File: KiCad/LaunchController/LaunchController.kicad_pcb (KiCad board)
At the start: 2 copper layers, 150 x 100 mm, 162 parts, among them J1 CONN_ICSP, J10 CONN_AUDIO, J11 RJ45, J12 CONN_SPEAKER, J2 CONN_USB, J3 USB_B_Micro, J4 DC_IN, J5 TO_CONVERTER, J6 FROM_CONVERTER, J7 CONN_STATUS_PANEL, J8 CONN_PANEL_BAORD_2, J9 CONN_PANEL_BAORD_1, Q1 TJ8S06M3L, Q2 TJ8S06M3L, Q3 2SC3325-Y, SW1 SW_Push, SW11 SW_Push, SW12 SW_Push, SW13 SW_Push, SW14 SW_Push, SW15 SW_Push, SW16 SW_Push, SW17 SW_Push, SW18 SW_Push, SW19 SW_Push, SW2 SW_Push, SW20 SW_Push, SW21 SW_Push, SW22 SW_Push, SW23 SW_Push, SW24 SW_Push, SW25 SW_Push, U1 FT232RL, U2 ATMEGA2560-16AUR, U3 NJM7805SDL1, U4 INA219BIDCNT, U5 INA219BIDCNT, U6 DFPlayer, U7 24LC256, U8 LTC485CN8#PBF, Y1 HUSG-16.000-20

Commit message: ロードスイッチ駆動用のトランジスタのベース抵抗を10kRに修正
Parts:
- R14: value 22kR -> 10kR
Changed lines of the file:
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@@
         (effects (font (size 1 1) (thickness 0.15)))
     )
-    (fp_text value "22kR" (at 0 1.43 180) (layer "F.Fab")
+    (fp_text value "10kR" (at 0 1.43 180) (layer "F.Fab")
         (effects (font (size 1 1) (thickness 0.15)))
     )

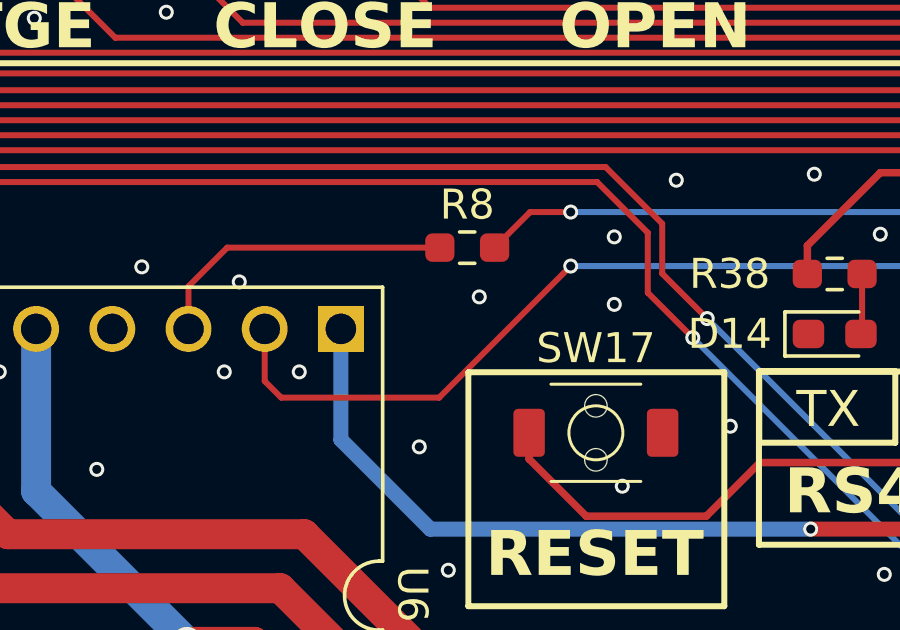
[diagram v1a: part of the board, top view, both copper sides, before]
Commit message: DFPlayerのTXにも抵抗を追加
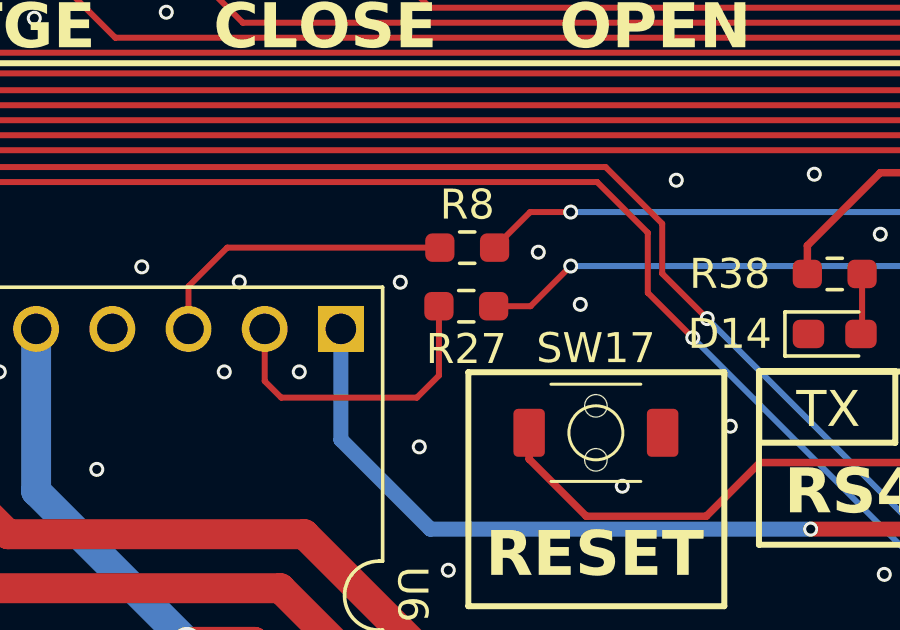
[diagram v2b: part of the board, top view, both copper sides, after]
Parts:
- added R27: 1kR, Resistor_SMD:R_0603_1608Metric_Pad0.98x0.95mm_HandSolder, F.Cu at (73.2, 88.2)
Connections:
- U2 pad 13: UART2_TX -> Net-(U2-PH1)
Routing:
- net UART2_TX: track 84.5 -> 10.4 mm, vias 2 -> 0
- net Net-(U2-PH1): track 0.00 -> 73.6 mm, vias 0 -> 2
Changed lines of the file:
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@@
   (net 165 "CONN_LED_POWER")
   (net 166 "CONN_LED_FB_SHIFT")
+  (net 167 "Net-(U2-PH1)")
   (footprint "Capacitor_SMD:C_0603_1608Metric_Pad1.08x0.95mm_HandSolder" (layer "F.Cu")
     (at 109.840587 69.251913 45)
@@
       (net 60 "Net-(U2-PH0)") (pinfunction "PH0") (pintype "bidirectional"))
     (pad "13" smd roundrect (at -7.6625 0 225) (size 1.475 0.3) (layers "F.Cu" "F.Paste" "F.Mask") (roundrect_rratio 0.25)
-      (net 100 "UART2_TX") (pinfunction "PH1") (pintype "bidirectional"))
+      (net 167 "Net-(U2-PH1)") (pinfunction "PH1") (pintype "bidirectional"))
     (pad "14" smd roundrect (at -7.6625 0.5 225) (size 1.475 0.3) (layers "F.Cu" "F.Paste" "F.Mask") (roundrect_rratio 0.25)
       (net 79 "CONN_LED_FB_PURGE") (pinfunction "PH2") (pintype "bidirectional"))
@@
     )
   )
+  (footprint "Resistor_SMD:R_0603_1608Metric_Pad0.98x0.95mm_HandSolder" (layer "F.Cu")
+    (at 73.2 88.2 180)
+    (descr "Resistor SMD 0603 (1608 Metric), square (rectangular) end terminal, IPC_7351 nominal with elongated pad for handsoldering. (Body size source: IPC-SM-782 page 72, https://www.pcb-3d.com/wordpress/wp-content/uploads/ipc-sm-782a_amendment_1_and_2.pdf), generated with kicad-footprint-generator")
+    (tags "resistor handsolder")
+    (property "LCSC" "")
+    (property "Sheetfile" "LaunchController.kicad_sch")
+    (property "Sheetname" "")
+    (property "ki_description" "Resistor, small symbol")
+    (property "ki_keywords" "R resistor")
+    (attr smd)
+    (fp_text reference "R27" (at 0 -1.43) (layer "F.SilkS")
+        (effects (font (size 1 1) (thickness 0.15)))
+    )
+    (fp_text value "1kR" (at 0 1.43) (layer "F.Fab")
+        (effects (font (size 1 1) (thickness 0.15)))
+    )
+    (fp_text user "${REFERENCE}" (at 0 0) (layer "F.Fab")
+        (effects (font (size 0.4 0.4) (thickness 0.06)))
+    )
+    (fp_line (start -0.254724 -0.5225) (end 0.254724 -0.5225)
+      (stroke (width 0.12) (type solid)) (layer "F.SilkS"))
+    (fp_line (start -0.254724 0.5225) (end 0.254724 0.5225)
+      (stroke (width 0.12) (type solid)) (layer "F.SilkS"))
+    (fp_line (start -1.65 -0.73) (end 1.65 -0.73)
+      (stroke (width 0.05) (type solid)) (layer "F.CrtYd"))
+    (fp_line (start -1.65 0.73) (end -1.65 -0.73)
+      (stroke (width 0.05) (type solid)) (layer "F.CrtYd"))
+    (fp_line (start 1.65 -0.73) (end 1.65 0.73)
+      (stroke (width 0.05) (type solid)) (layer "F.CrtYd"))
+    (fp_line (start 1.65 0.73) (end -1.65 0.73)
+      (stroke (width 0.05) (type solid)) (layer "F.CrtYd"))
+    (fp_line (start -0.8 -0.4125) (end 0.8 -0.4125)
+      (stroke (width 0.1) (type solid)) (layer "F.Fab"))
+    (fp_line (start -0.8 0.4125) (end -0.8 -0.4125)
+      (stroke (width 0.1) (type solid)) (layer "F.Fab"))
+    (fp_line (start 0.8 -0.4125) (end 0.8 0.4125)
+      (stroke (width 0.1) (type solid)) (layer "F.Fab"))
+    (fp_line (start 0.8 0.4125) (end -0.8 0.4125)
+      (stroke (width 0.1) (type solid)) (layer "F.Fab"))
+    (pad "1" smd roundrect (at -0.9125 0 180) (size 0.975 0.95) (layers "F.Cu" "F.Paste" "F.Mask") (roundrect_rratio 0.25)
+      (net 167 "Net-(U2-PH1)") (pintype "passive"))
+    (pad "2" smd roundrect (at 0.9125 0 180) (size 0.975 0.95) (layers "F.Cu" "F.Paste" "F.Mask") (roundrect_rratio 0.25)
+      (net 100 "UART2_TX") (pintype "passive"))
+    (model "${KICAD6_3DMODEL_DIR}/Resistor_SMD.3dshapes/R_0603_1608Metric.wrl"
+      (offset (xyz 0 0 0))
+      (scale (xyz 1 1 1))
+      (rotate (xyz 0 0 0))
+    )
+  )
   (footprint "LED_SMD:LED_0603_1608Metric_Pad1.05x0.95mm_HandSolder" (layer "F.Cu")
     (at 76.735 75.75 90)
@@
   (via (at 139.4 47.4) (size 0.5) (drill 0.3) (layers "F.Cu" "B.Cu") (free) (net 1))
   (via (at 103 104.25) (size 0.5) (drill 0.3) (layers "F.Cu" "B.Cu") (free) (net 1))
-  (via (at 78.133174 85.888716) (size 0.5) (drill 0.3) (layers "F.Cu" "B.Cu") (free) (net 1))
+  (via (at 75.6 86.4) (size 0.5) (drill 0.3) (layers "F.Cu" "B.Cu") (free) (net 1))
   (via (at 58.8 78.6) (size 0.5) (drill 0.3) (layers "F.Cu" "B.Cu") (free) (net 1))
   (via (at 122.883174 107.638716) (size 0.5) (drill 0.3) (layers "F.Cu" "B.Cu") (free) (net 1))
@@
   (via (at 94.6 47.2) (size 0.5) (drill 0.3) (layers "F.Cu" "B.Cu") (free) (net 1))
   (via (at 165.883174 90.138716) (size 0.5) (drill 0.3) (layers "F.Cu" "B.Cu") (free) (net 1))
-  (via (at 78.133174 88.138716) (size 0.5) (drill 0.3) (layers "F.Cu" "B.Cu") (free) (net 1))
+  (via (at 77 88.138716) (size 0.5) (drill 0.3) (layers "F.Cu" "B.Cu") (free) (net 1))
   (via (at 123.883174 92.638716) (size 0.5) (drill 0.3) (layers "F.Cu" "B.Cu") (free) (net 1))
   (via (at 158.383174 129.138716) (size 0.5) (drill 0.3) (layers "F.Cu" "B.Cu") (free) (net 1))
@@
   (via (at 91 50.6) (size 0.5) (drill 0.3) (layers "F.Cu" "B.Cu") (free) (net 1))
   (via (at 55.133174 104.638716) (size 0.5) (drill 0.3) (layers "F.Cu" "B.Cu") (free) (net 1))
-  (via (at 73.633174 87.888716) (size 0.5) (drill 0.3) (layers "F.Cu" "B.Cu") (free) (net 1))
+  (via (at 71 87.4) (size 0.5) (drill 0.3) (layers "F.Cu" "B.Cu") (free) (net 1))
   (via (at 72.2 69.8) (size 0.5) (drill 0.3) (layers "F.Cu" "B.Cu") (free) (net 1))
   (via (at 106.6 69.4) (size 0.5) (drill 0.3) (layers "F.Cu" "B.Cu") (free) (net 1))
@@
   (segment (start 129.182676 63) (end 130.230707 64.048031) (width 0.2) (layer "B.Cu") (net 88))
   (segment (start 82.4 68.8) (end 82.4 68.784315) (width 0.2) (layer "B.Cu") (net 88))
-  (segment (start 130.994263 72.483237) (end 128.048913 75.428587) (width 0.2) (layer "F.Cu") (net 100))
-  (segment (start 67.030707 91.246793) (end 66.480707 90.696793) (width 0.2) (layer "F.Cu") (net 100))
-  (segment (start 76.680707 86.861793) (end 72.295707 91.246793) (width 0.2) (layer "F.Cu") (net 100))
-  (segment (start 130.994263 72.098237) (end 130.994263 72.483237) (width 0.2) (layer "F.Cu") (net 100))
-  (segment (start 72.295707 91.246793) (end 67.030707 91.246793) (width 0.2) (layer "F.Cu") (net 100))
   (segment (start 66.480707 90.696793) (end 66.480707 88.956793) (width 0.2) (layer "F.Cu") (net 100))
-  (via (at 76.680707 86.861793) (size 0.5) (drill 0.3) (layers "F.Cu" "B.Cu") (net 100))
-  (via (at 130.994263 72.098237) (size 0.5) (drill 0.3) (layers "F.Cu" "B.Cu") (net 100))
-  (segment (start 130.994263 72.098237) (end 130.994263 71.875349) (width 0.2) (layer "B.Cu") (net 100))
-  (segment (start 116.130707 65.611793) (end 94.880707 86.861793) (width 0.2) (layer "B.Cu") (net 100))
-  (segment (start 130.994263 71.875349) (end 124.730707 65.611793) (width 0.2) (layer "B.Cu") (net 100))
-  (segment (start 124.730707 65.611793) (end 116.130707 65.611793) (width 0.2) (layer "B.Cu") (net 100))
-  (segment (start 94.880707 86.861793) (end 76.680707 86.861793) (width 0.2) (layer "B.Cu") (net 100))
+  (segment (start 72.2875 88.2) (end 72.2875 90.5125) (width 0.2) (layer "F.Cu") (net 100))
+  (segment (start 71.553207 91.246793) (end 67.030707 91.246793) (width 0.2) (layer "F.Cu") (net 100))
+  (segment (start 67.030707 91.246793) (end 66.480707 90.696793) (width 0.2) (layer "F.Cu") (net 100))
+  (segment (start 72.2875 90.5125) (end 71.553207 91.246793) (width 0.2) (layer "F.Cu") (net 100))
   (segment (start 112.181707 75.34754) (end 114.720478 77.886311) (width 0.2) (layer "F.Cu") (net 109))
   (segment (start 112.181707 74.112293) (end 112.181707 75.34754) (width 0.2) (layer "F.Cu") (net 109))
@@
   (segment (start 137.480707 61.861793) (end 137.480707 69.861793) (width 0.2) (layer "B.Cu") (net 166))
   (segment (start 132.709457 57.090543) (end 137.480707 61.861793) (width 0.2) (layer "B.Cu") (net 166))
+  (segment (start 76.680707 86.861793) (end 75.3425 88.2) (width 0.2) (layer "F.Cu") (net 167))
+  (segment (start 130.994263 72.483237) (end 128.048913 75.428587) (width 0.2) (layer "F.Cu") (net 167))
+  (segment (start 130.994263 72.098237) (end 130.994263 72.483237) (width 0.2) (layer "F.Cu") (net 167))
+  (segment (start 75.3425 88.2) (end 74.1125 88.2) (width 0.2) (layer "F.Cu") (net 167))
+  (via (at 76.680707 86.861793) (size 0.5) (drill 0.3) (layers "F.Cu" "B.Cu") (net 167))
+  (via (at 130.994263 72.098237) (size 0.5) (drill 0.3) (layers "F.Cu" "B.Cu") (net 167))
+  (segment (start 130.994263 72.098237) (end 130.994263 71.875349) (width 0.2) (layer "B.Cu") (net 167))
+  (segment (start 116.130707 65.611793) (end 94.880707 86.861793) (width 0.2) (layer "B.Cu") (net 167))
+  (segment (start 130.994263 71.875349) (end 124.730707 65.611793) (width 0.2) (layer "B.Cu") (net 167))
+  (segment (start 124.730707 65.611793) (end 116.130707 65.611793) (width 0.2) (layer "B.Cu") (net 167))
+  (segment (start 94.880707 86.861793) (end 76.680707 86.861793) (width 0.2) (layer "B.Cu") (net 167))
   (zone locked (net 0) (net_name "") (layer "F.Cu") (hatch edge 0.5)
     (connect_pads (clearance 0))

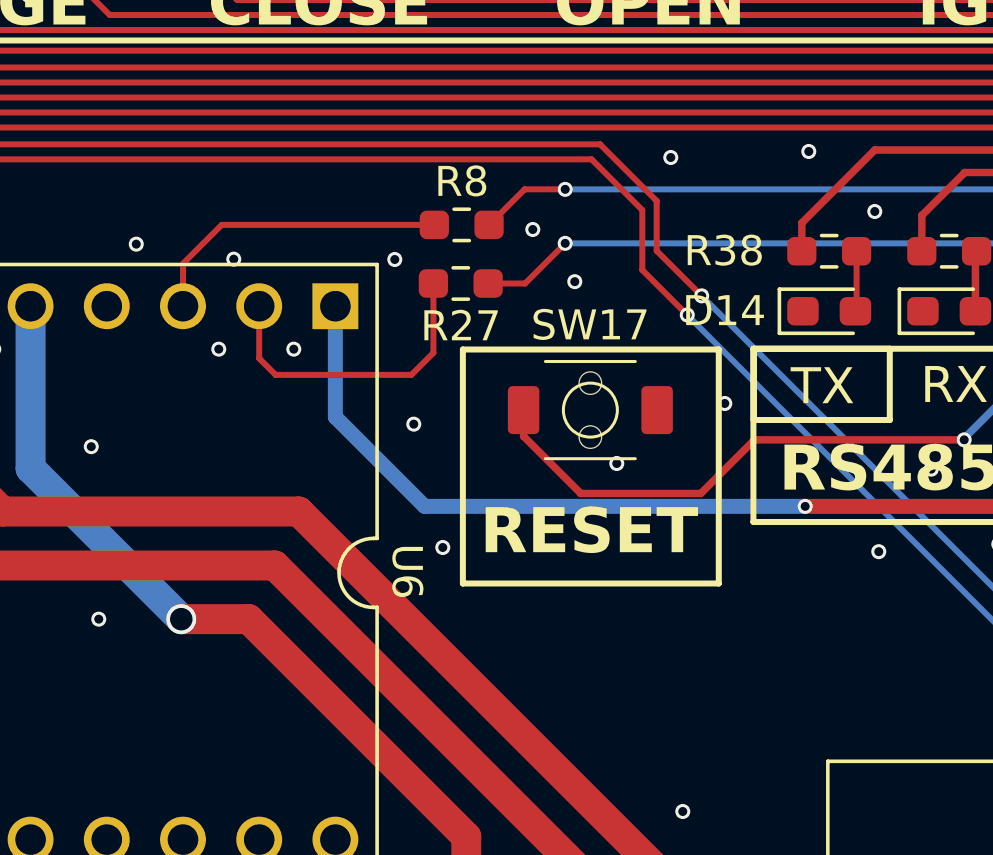
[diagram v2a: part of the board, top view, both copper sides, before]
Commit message: 敗北ダイオードを追加
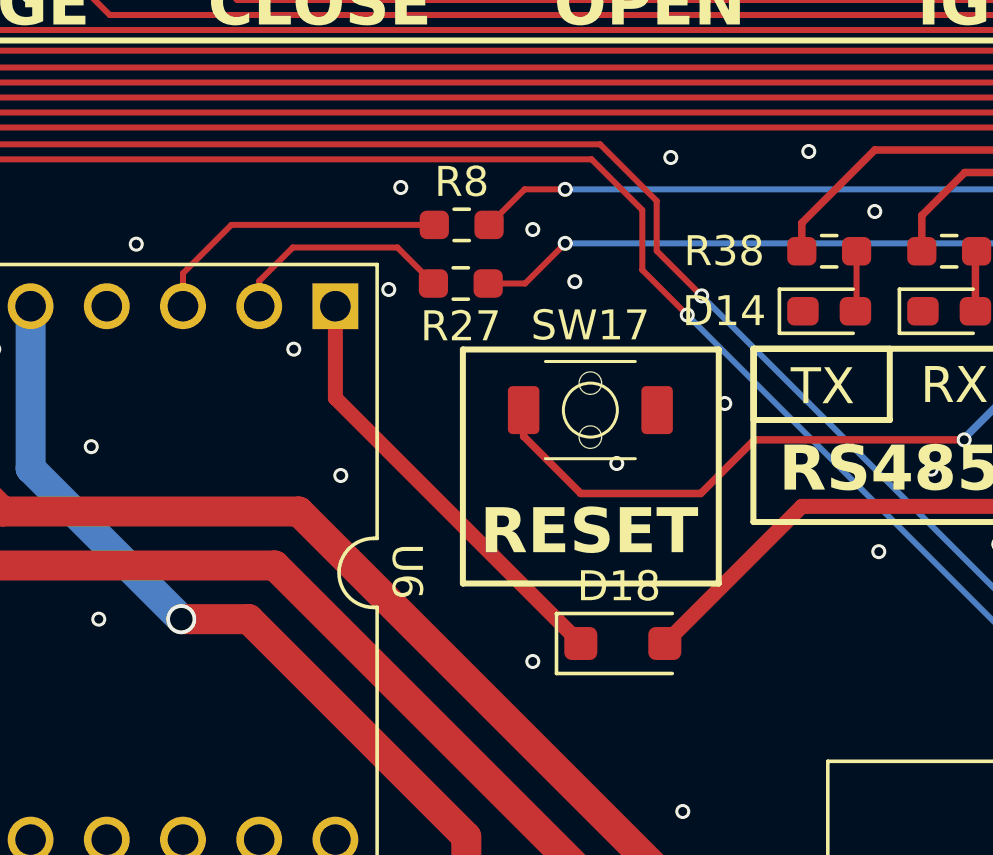
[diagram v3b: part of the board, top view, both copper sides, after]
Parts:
- added D18: GS1010FL, Diode_SMD:D_SOD-123F, F.Cu at (78.6, 100.2)
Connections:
- U6 pad 1: CONN_LED_5V -> Net-(D18-K)
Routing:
- net Net-(D18-K): track 0.00 -> 14.6 mm
- net CONN_LED_5V: track 637.7 -> 623.7 mm, vias 10 -> 9
- net UART2_TX: track 10.4 -> 7.60 mm
- net GND: vias 284 -> 283
